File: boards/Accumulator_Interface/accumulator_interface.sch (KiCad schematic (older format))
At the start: 0 parts

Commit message: added more connections to the accumulator schematic
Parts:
- added J?: INTERNAL, footprints:Ultrafit_4, symbol Ultrafit_4
- added J?: DISCHARGE, footprints:Ultrafit_2, symbol Ultrafit_2
- added J?: BMS_MASTER, footprints:Ultrafit_2, symbol Ultrafit_2
- added J?: AIR_CTRL, footprints:Ultrafit_2, symbol Ultrafit_2
- added J?: IMD_LATCH, footprints:Ultrafit_2, symbol Ultrafit_2
- added J?: TSAL/AIL, footprints:micromatch_female_vert_4, symbol micromatch_female_TOP_ENTRY_locking_4
- added J?: EXTERNAL, symbol Ampseal_35
- added J?: IMD_LATCH, footprints:micromatch_female_vert_4, symbol micromatch_female_TOP_ENTRY_locking_4
- added J?: AIR_CTRL_18, footprints:micromatch_female_vert_18, symbol micromatch_female_TOP_ENTRY_locking_18
- added J?: BMS, footprints:micromatch_female_vert_14, symbol micromatch_female_TOP_ENTRY_locking_14
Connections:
- new net 12V: J?.15, J?.2, J?.2, J?.2, J?.2, J?.26
- new net AIR_CTRL_5V_OUT: J?.3
- new net AIR_CTRL_LED_1: J?.10
- new net AIR_CTRL_LED_2: J?.11
- new net AIR_CTRL_RESET: J?.7
- new net BMS_5V_OUT: J?.3
- new net BMS_IN/IMD_LATCH_OUT: J?.1, J?.12, J?.2
- new net BMS_LED_1: J?.10
- new net BMS_LED_2: J?.11
- new net BMS_RESET: J?.7
- new net BMS_STATUS: J?.13, J?.16
- new net BSPD_CURRENT_SENSE: J?.14, J?.27
- new net CAN_HIGH: J?.13, J?.24, J?.8, J?.8
- new net CAN_LOW: J?.14, J?.25, J?.9, J?.9
- new net CRASH_IN/HVD_OUT: J?.1, J?.28
- new net FAN_12V: J?.7, J?.8, J?.9
- new net FAN_GND: J?.4, J?.5, J?.6
- new net FAN_PWM: J?.10, J?.11, J?.12, J?.12
- new net GND: J?.1, J?.1, J?.1, J?.1, J?.1, J?.2, J?.2, J?.3
- new net HVD_IN/MAIN_PACK_OUT: J?.15, J?.2, J?.3
- new net HVD_IN/TSMS_OUT: J?.30, J?.31
- new net IMD_LATCH_IN/HVD_OUT: J?.13, J?.2, J?.29
- new net IMD_LATCH_STATUS: J?.17, J?.3
- new net MAIN_PACK_IN/BMS_OUT: J?.1, J?.14, J?.4
- new net MISO: J?.5, J?.5
- new net MOSI: J?.4, J?.4
- new net SCK: J?.6, J?.6
- new net TSAL+: J?.3, J?.34
- new net TSAL-: J?.35, J?.4
- new net TSMS_IN: J?.1, J?.1, J?.32

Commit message: Accum Interface Update
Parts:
- added U?: RJ45_VT_BMS, footprints:RJ45-Vertical, symbol RJ45_VT
- added U?: RJ45_VT_AIR, footprints:RJ45-Vertical, symbol RJ45_VT
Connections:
- net AIR_CTRL_5V_OUT: now also U?.7 (5V)
- net AIR_CTRL_LED_1: now also U?.10 (LED_1)
- net AIR_CTRL_LED_2: now also U?.12 (LED_2)
- net BMS_5V_OUT: now also U?.7 (5V)
- net BMS_LED_1: now also U?.10 (LED_1)
- net BMS_LED_2: now also U?.12 (LED_2)
- net BMS_RESET: now also U?.3 (RESET)
- net CAN_HIGH: now also U?.2 (CANH), U?.2 (CANH)
- net CAN_LOW: now also U?.1 (CANL), U?.1 (CANL)
- net GND: now also J?.4, U?.11 (GND), U?.11 (GND), U?.13 (GND), U?.13 (GND), U?.14 (GND), U?.14 (GND), U?.8 (GND), U?.8 (GND), U?.9 (GND), U?.9 (GND)
- net MISO renamed MISO_AIR
- net MISO_AIR: now also U?.5 (MISO); no longer J?.5
- net MOSI renamed MOSI_AIR
- net MOSI_AIR: now also U?.6 (MOSI); no longer J?.4
- net SCK renamed SCK_AIR
- net SCK_AIR: now also U?.4 (SCK); no longer J?.6
- new net MISO_BMS: J?.5, U?.5 (MISO)
- new net MOSI_BMS: J?.4, U?.6 (MOSI)
- new net SCK_BMS: J?.6, U?.4 (SCK)
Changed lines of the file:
@@
 AIR_CTRL_5V_OUT
 Text Label 5050 2550 0    60   ~ 0
-MOSI
+MOSI_AIR
 Text Label 5050 2650 0    60   ~ 0
-MISO
+MISO_AIR
 Text Label 5050 2750 0    60   ~ 0
-SCK
+SCK_AIR
 Text Label 5050 2850 0    60   ~ 0
 AIR_CTRL_RESET
@@
 BMS_5V_OUT
 Text Label 5050 4600 0    60   ~ 0
-MOSI
+MOSI_BMS
 Text Label 5050 4700 0    60   ~ 0
-MISO
+MISO_BMS
 Text Label 5050 4800 0    60   ~ 0
-SCK
+SCK_BMS
 Text Label 5050 4900 0    60   ~ 0
 BMS_RESET
@@
 Text Label 5050 5600 0    60   ~ 0
 BSPD_CURRENT_SENSE
+Text Label 5050 1900 0    60   ~ 0
+GND
+$Comp
+L RJ45_VT U?
+U 1 1 5A791FDB
+P 3075 3635
+F 0 "U?" H 3075 3045 60  0000 C CNN
+F 1 "RJ45_VT_BMS" H 3085 4295 60  0000 C CNN
+F 2 "footprints:RJ45-Vertical" H 2975 2945 60  0001 C CNN
+F 3 "" H 3075 3045 60  0001 C CNN
+	1    3075 3635
+	1    0    0    -1
+$EndComp
+Text Label 3475 4025 3    60   ~ 0
+GND
+Text Label 3585 4025 3    60   ~ 0
+GND
+Text Label 3175 4025 3    60   ~ 0
+GND
+Text Label 3925 3505 0    60   ~ 0
+GND
+Text Label 2895 4025 3    60   ~ 0
+GND
+Text Label 3925 3405 0    60   ~ 0
+BMS_5V_OUT
+Text Label 3925 3305 0    60   ~ 0
+MOSI_BMS
+Text Label 3925 3205 0    60   ~ 0
+MISO_BMS
+Text Label 3005 4025 3    60   ~ 0
+BMS_LED_1
+Text Label 3285 4025 3    60   ~ 0
+BMS_LED_2
+Text Label 2595 3405 2    60   ~ 0
+BMS_RESET
+Text Label 2595 3205 2    60   ~ 0
+CAN_LOW
+Text Label 2595 3305 2    60   ~ 0
+CAN_HIGH
+$Comp
+L RJ45_VT U?
+U 1 1 5A793BC8
+P 2955 5420
+F 0 "U?" H 2955 4830 60  0000 C CNN
+F 1 "RJ45_VT_AIR" H 2965 6080 60  0000 C CNN
+F 2 "footprints:RJ45-Vertical" H 2855 4730 60  0001 C CNN
+F 3 "" H 2955 4830 60  0001 C CNN
+	1    2955 5420
+	1    0    0    -1
+$EndComp
+Text Label 3355 5810 3    60   ~ 0
+GND
+Text Label 3465 5810 3    60   ~ 0
+GND
+Text Label 3055 5810 3    60   ~ 0
+GND
+Text Label 3805 5290 0    60   ~ 0
+GND
+Text Label 2775 5810 3    60   ~ 0
+GND
+Text Label 2475 4990 2    60   ~ 0
+CAN_LOW
+Text Label 2475 5090 2    60   ~ 0
+CAN_HIGH
+Text Label 2595 3505 2    60   ~ 0
+SCK_BMS
+Text Label 2475 5290 2    60   ~ 0
+SCK_AIR
+Text Label 2885 5810 3    60   ~ 0
+AIR_CTRL_LED_1
+Text Label 3165 5810 3    60   ~ 0
+AIR_CTRL_LED_2
+Text Label 3805 4990 0    60   ~ 0
+MISO_AIR
+Text Label 3805 5090 0    60   ~ 0
+MOSI_AIR
+Text Label 3805 5190 0    60   ~ 0
+AIR_CTRL_5V_OUT
 $EndSCHEMATC

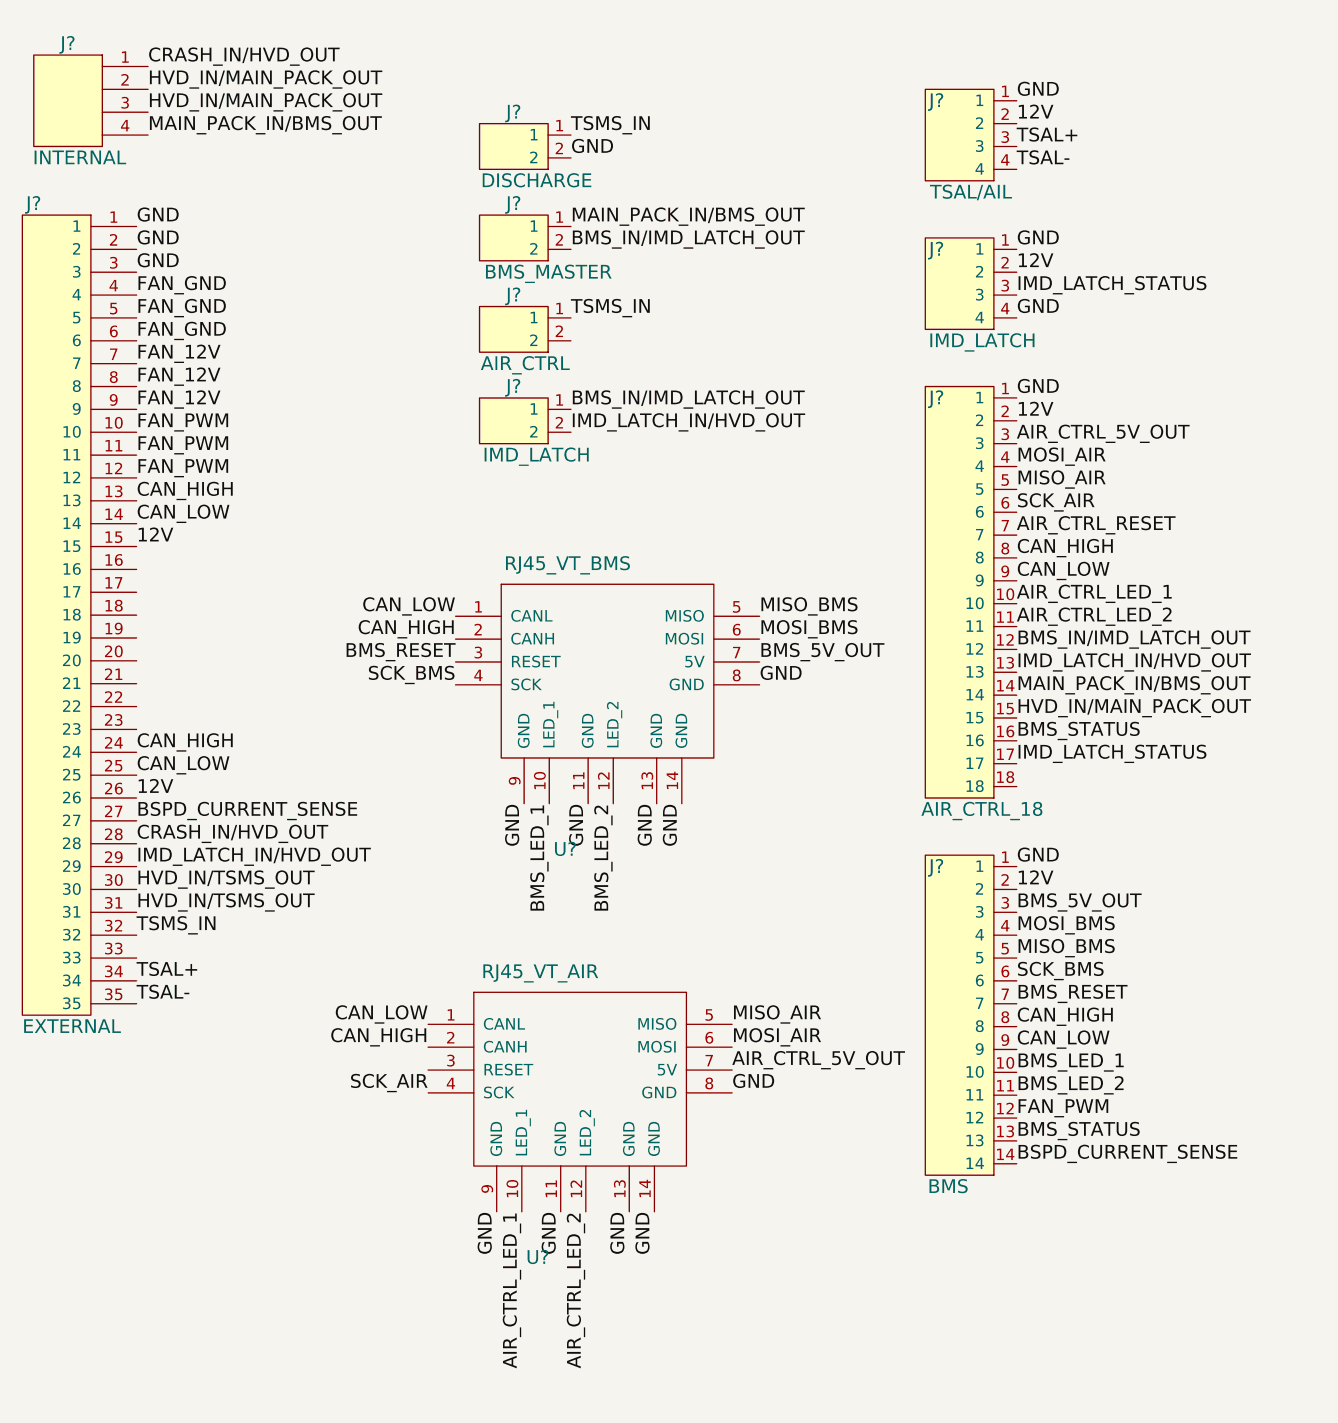
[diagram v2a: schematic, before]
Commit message: add accumulator connector
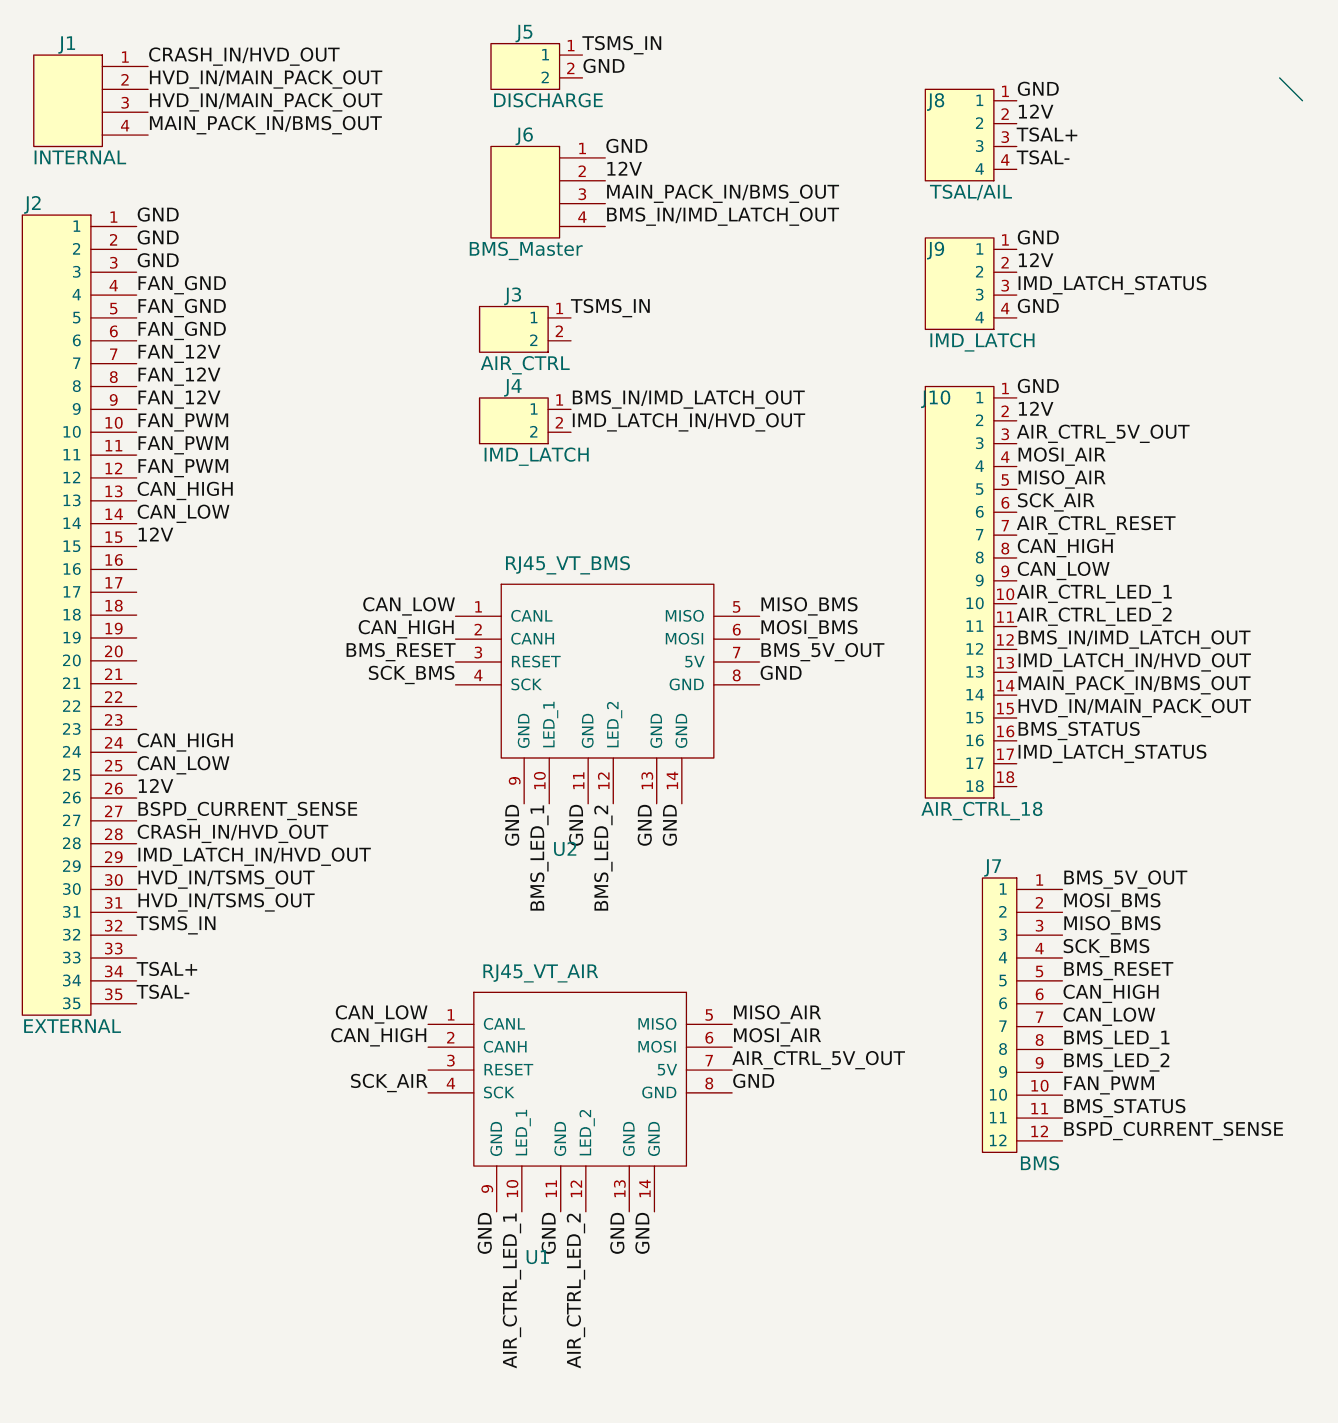
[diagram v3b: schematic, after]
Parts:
- removed J?: BMS_MASTER, footprints:Ultrafit_2, symbol Ultrafit_2
- removed J?: BMS, footprints:micromatch_female_vert_14, symbol micromatch_female_TOP_ENTRY_locking_14
- added J6: BMS_Master, footprints:Ultrafit_4, symbol Ultrafit_4
- added J7: BMS, symbol MicroFit_12
- gave numbers to parts that had none: 10
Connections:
- net 12V: now also J6.2
- net BMS_5V_OUT: now also J7.1
- net BMS_IN/IMD_LATCH_OUT: now also J6.4
- net BMS_LED_1: now also J7.8
- net BMS_LED_2: now also J7.9
- net BMS_RESET: now also J7.5
- net BMS_STATUS: now also J7.11
- net BSPD_CURRENT_SENSE: now also J7.12
- net CAN_HIGH: now also J7.6
- net CAN_LOW: now also J7.7
- net FAN_PWM: now also J7.10
- net GND: now also J6.1
- net MAIN_PACK_IN/BMS_OUT: now also J6.3
- net MISO_BMS: now also J7.3
- net MOSI_BMS: now also J7.2
- net SCK_BMS: now also J7.4
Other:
- moved on the sheet: J5
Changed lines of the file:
@@
 $EndDescr
 $Comp
-L Ultrafit_4 J?
+L Ultrafit_4 J1
 U 1 1 5A7721C7
 P 900 1000
-F 0 "J?" H 900 1300 60  0000 C CNN
+F 0 "J1" H 900 1300 60  0000 C CNN
 F 1 "INTERNAL" H 950 800 60  0000 C CNN
 F 2 "footprints:Ultrafit_4" H 800 1250 60  0001 C CNN
@@
 $EndComp
 $Comp
-L Ultrafit_2 J?
+L Ultrafit_2 J5
 U 1 1 5A772294
-P 2850 1150
-F 0 "J?" H 2850 1300 60  0000 C CNN
-F 1 "DISCHARGE" H 2950 1000 60  0000 C CNN
-F 2 "footprints:Ultrafit_2" H 2750 1200 60  0001 C CNN
-F 3 "" H 2850 1300 60  0001 C CNN
-F 4 "https://www.digikey.com/product-detail/en/molex-llc/1722861102/WM11570-ND/5344267" H 2950 1400 60  0001 C CNN "PurchasingLink"
-F 5 "Digi-Key" H 3050 1500 60  0001 C CNN "MFN"
-F 6 "WM11570-ND" H 3150 1600 60  0001 C CNN "MPN"
-F 7 "Value" H 3250 1700 60  0001 C CNN "Package"
-	1    2850 1150
-	1    0    0    -1
-$EndComp
-Text Label 3100 1100 0    60   ~ 0
+P 2900 800
+F 0 "J5" H 2900 950 60  0000 C CNN
+F 1 "DISCHARGE" H 3000 650 60  0000 C CNN
+F 2 "footprints:Ultrafit_2" H 2800 850 60  0001 C CNN
+F 3 "" H 2900 950 60  0001 C CNN
+F 4 "https://www.digikey.com/product-detail/en/molex-llc/1722861102/WM11570-ND/5344267" H 3000 1050 60  0001 C CNN "PurchasingLink"
+F 5 "Digi-Key" H 3100 1150 60  0001 C CNN "MFN"
+F 6 "WM11570-ND" H 3200 1250 60  0001 C CNN "MPN"
+F 7 "Value" H 3300 1350 60  0001 C CNN "Package"
+	1    2900 800
+	1    0    0    -1
+$EndComp
+Text Label 3150 750  0    60   ~ 0
 TSMS_IN
-Text Label 3100 1200 0    60   ~ 0
+Text Label 3150 850  0    60   ~ 0
 GND
 Text Label 5050 950  0    60   ~ 0
@@
 Text Label 1250 1100 0    60   ~ 0
 MAIN_PACK_IN/BMS_OUT
-$Comp
-L Ultrafit_2 J?
-U 1 1 5A772BD8
-P 2850 1550
-F 0 "J?" H 2850 1700 60  0000 C CNN
-F 1 "BMS_MASTER" H 3000 1400 60  0000 C CNN
-F 2 "footprints:Ultrafit_2" H 2750 1600 60  0001 C CNN
-F 3 "" H 2850 1700 60  0001 C CNN
-F 4 "https://www.digikey.com/product-detail/en/molex-llc/1722861102/WM11570-ND/5344267" H 2950 1800 60  0001 C CNN "PurchasingLink"
-F 5 "Digi-Key" H 3050 1900 60  0001 C CNN "MFN"
-F 6 "WM11570-ND" H 3150 2000 60  0001 C CNN "MPN"
-F 7 "Value" H 3250 2100 60  0001 C CNN "Package"
-	1    2850 1550
-	1    0    0    -1
-$EndComp
-Text Label 3100 1500 0    60   ~ 0
+Text Label 3250 1400 0    60   ~ 0
 MAIN_PACK_IN/BMS_OUT
-Text Label 3100 1600 0    60   ~ 0
+Text Label 3250 1500 0    60   ~ 0
 BMS_IN/IMD_LATCH_OUT
 $Comp
-L Ultrafit_2 J?
+L Ultrafit_2 J3
 U 1 1 5A772C69
 P 2850 1950
-F 0 "J?" H 2850 2100 60  0000 C CNN
+F 0 "J3" H 2850 2100 60  0000 C CNN
 F 1 "AIR_CTRL" H 2900 1800 60  0000 C CNN
 F 2 "footprints:Ultrafit_2" H 2750 2000 60  0001 C CNN
@@
 TSMS_IN
 $Comp
-L Ultrafit_2 J?
+L Ultrafit_2 J4
 U 1 1 5A772CE5
 P 2850 2350
-F 0 "J?" H 2850 2500 60  0000 C CNN
+F 0 "J4" H 2850 2500 60  0000 C CNN
 F 1 "IMD_LATCH" H 2950 2200 60  0000 C CNN
 F 2 "footprints:Ultrafit_2" H 2750 2400 60  0001 C CNN
@@
 IMD_LATCH_IN/HVD_OUT
 $Comp
-L Ampseal_35 J?
+L Ampseal_35 J2
 U 1 1 5A77324C
 P 1000 3200
-F 0 "J?" H 750 5000 60  0000 C CNN
+F 0 "J2" H 750 5000 60  0000 C CNN
 F 1 "EXTERNAL" H 700 1400 60  0000 L CNN
 F 2 "" H 800 4550 60  0001 C CNN
@@
 TSAL-
 $Comp
-L micromatch_female_TOP_ENTRY_locking_4 J?
+L micromatch_female_TOP_ENTRY_locking_4 J8
 U 1 1 5A7731E9
 P 4800 1150
-F 0 "J?" H 4700 1350 60  0000 C CNN
+F 0 "J8" H 4700 1350 60  0000 C CNN
 F 1 "TSAL/AIL" H 4850 950 60  0000 C CNN
 F 2 "footprints:micromatch_female_vert_4" H 4600 2250 60  0001 C CNN
@@
 $EndComp
 $Comp
-L micromatch_female_TOP_ENTRY_locking_4 J?
+L micromatch_female_TOP_ENTRY_locking_4 J9
 U 1 1 5A7733D7
 P 4800 1800
-F 0 "J?" H 4700 2000 60  0000 C CNN
+F 0 "J9" H 4700 2000 60  0000 C CNN
 F 1 "IMD_LATCH" H 4900 1600 60  0000 C CNN
 F 2 "footprints:micromatch_female_vert_4" H 4600 2900 60  0001 C CNN
@@
 IMD_LATCH_STATUS
 $Comp
-L micromatch_female_TOP_ENTRY_locking_18 J?
+L micromatch_female_TOP_ENTRY_locking_18 J10
 U 1 1 5A773706
 P 4900 3350
-F 0 "J?" H 4700 4450 60  0000 C CNN
+F 0 "J10" H 4700 4450 60  0000 C CNN
 F 1 "AIR_CTRL_18" H 4900 2650 60  0000 C CNN
 F 2 "footprints:micromatch_female_vert_18" H 4700 4450 60  0001 C CNN
@@
 Text Label 5050 3850 0    60   ~ 0
 IMD_LATCH_STATUS
-$Comp
-L micromatch_female_TOP_ENTRY_locking_14 J?
-U 1 1 5A77471D
-P 4750 4950
-F 0 "J?" H 4700 5600 60  0000 C CNN
-F 1 "BMS" H 4750 4200 60  0000 C CNN
-F 2 "footprints:micromatch_female_vert_14" H 4700 5600 60  0001 C CNN
-F 3 "" H 4800 5700 60  0001 C CNN
-F 4 "https://www.digikey.com/product-detail/en/te-connectivity-amp-connectors/1-338068-4/A99502CT-ND/1955735" H 4750 6250 60  0001 C CNN "PurchasingLink"
-F 5 "Digi-Key" H 4850 6350 60  0001 C CNN "MFN"
-F 6 "A99502CT-ND" H 4950 6450 60  0001 C CNN "MPN"
-F 7 "Value" H 5050 6550 60  0001 C CNN "Package"
-	1    4750 4950
-	1    0    0    -1
-$EndComp
-Text Label 5050 4300 0    60   ~ 0
-GND
-Text Label 5050 4400 0    60   ~ 0
-12V
-Text Label 5050 4500 0    60   ~ 0
+Text Label 5250 4400 0    60   ~ 0
 BMS_5V_OUT
-Text Label 5050 4600 0    60   ~ 0
+Text Label 5250 4500 0    60   ~ 0
 MOSI_BMS
-Text Label 5050 4700 0    60   ~ 0
+Text Label 5250 4600 0    60   ~ 0
 MISO_BMS
-Text Label 5050 4800 0    60   ~ 0
+Text Label 5250 4700 0    60   ~ 0
 SCK_BMS
-Text Label 5050 4900 0    60   ~ 0
+Text Label 5250 4800 0    60   ~ 0
 BMS_RESET
-Text Label 5050 5000 0    60   ~ 0
-CAN_HIGH
-Text Label 5050 5100 0    60   ~ 0
-CAN_LOW
-Text Label 5050 5200 0    60   ~ 0
+Text Label 5250 4900 0    60   ~ 0
+CAN_HIGH
+Text Label 5250 5000 0    60   ~ 0
+CAN_LOW
+Text Label 5250 5100 0    60   ~ 0
 BMS_LED_1
-Text Label 5050 5300 0    60   ~ 0
+Text Label 5250 5200 0    60   ~ 0
 BMS_LED_2
-Text Label 5050 5400 0    60   ~ 0
+Text Label 5250 5300 0    60   ~ 0
 FAN_PWM
-Text Label 5050 5500 0    60   ~ 0
+Text Label 5250 5400 0    60   ~ 0
 BMS_STATUS
-Text Label 5050 5600 0    60   ~ 0
+Text Label 5250 5500 0    60   ~ 0
 BSPD_CURRENT_SENSE
 Text Label 5050 1900 0    60   ~ 0
 GND
 $Comp
-L RJ45_VT U?
+L RJ45_VT U2
 U 1 1 5A791FDB
 P 3075 3635
-F 0 "U?" H 3075 3045 60  0000 C CNN
+F 0 "U2" H 3075 3045 60  0000 C CNN
 F 1 "RJ45_VT_BMS" H 3085 4295 60  0000 C CNN
 F 2 "footprints:RJ45-Vertical" H 2975 2945 60  0001 C CNN
@@
 CAN_HIGH
 $Comp
-L RJ45_VT U?
+L RJ45_VT U1
 U 1 1 5A793BC8
 P 2955 5420
-F 0 "U?" H 2955 4830 60  0000 C CNN
+F 0 "U1" H 2955 4830 60  0000 C CNN
 F 1 "RJ45_VT_AIR" H 2965 6080 60  0000 C CNN
 F 2 "footprints:RJ45-Vertical" H 2855 4730 60  0001 C CNN
@@
 Text Label 3805 5190 0    60   ~ 0
 AIR_CTRL_5V_OUT
+$Comp
+L Ultrafit_4 J6
+U 1 1 5A7D1779
+P 2900 1400
+F 0 "J6" H 2900 1700 60  0000 C CNN
+F 1 "BMS_Master" H 2900 1200 60  0000 C CNN
+F 2 "footprints:Ultrafit_4" H 2800 1650 60  0001 C CNN
+F 3 "http://www.literature.molex.com/SQLImages/kelmscott/Molex/PDF_Images/987651-1008.pdf" H 2900 1750 60  0001 C CNN
+F 4 "Digi-Key" H 2900 1400 60  0001 C CNN "MFN"
+F 5 "Value" H 2900 1400 60  0001 C CNN "Package"
+F 6 "WM11574-ND" H 2900 1400 60  0001 C CNN "MPN"
+F 7 "WM11564-ND" H 3300 2150 60  0001 C CNN "MPN2"
+F 8 "https://www.digikey.com/products/en?keywords=WM11574-ND" H 3400 2250 60  0001 C CNN "PurchasingLink"
+F 9 "https://www.digikey.com/product-detail/en/molex-llc/1722561004/WM11564-ND/5291228" H 3500 2350 60  0001 C CNN "PurchasingLink2"
+	1    2900 1400
+	1    0    0    -1
+$EndComp
+Entry Wire Line
+	6200 850  6300 950
+Text Label 3250 1200 0    60   ~ 0
+GND
+Text Label 3250 1300 0    60   ~ 0
+12V
+$Comp
+L MicroFit_12 J7
+U 1 1 5A7D1B20
+P 4700 4200
+F 0 "J7" H 4950 4100 60  0000 C CNN
+F 1 "BMS" H 5150 2800 60  0000 C CNN
+F 2 "" H 4700 4200 60  0001 C CNN
+F 3 "" H 4700 4200 60  0001 C CNN
+	1    4700 4200
+	1    0    0    -1
+$EndComp
 $EndSCHEMATC
